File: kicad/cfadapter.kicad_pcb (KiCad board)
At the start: 2 copper layers, 66.9 x 60.4 mm, 5 parts, among them CON1 CF-CARD, J1 Extension port, U1 GAL16V8

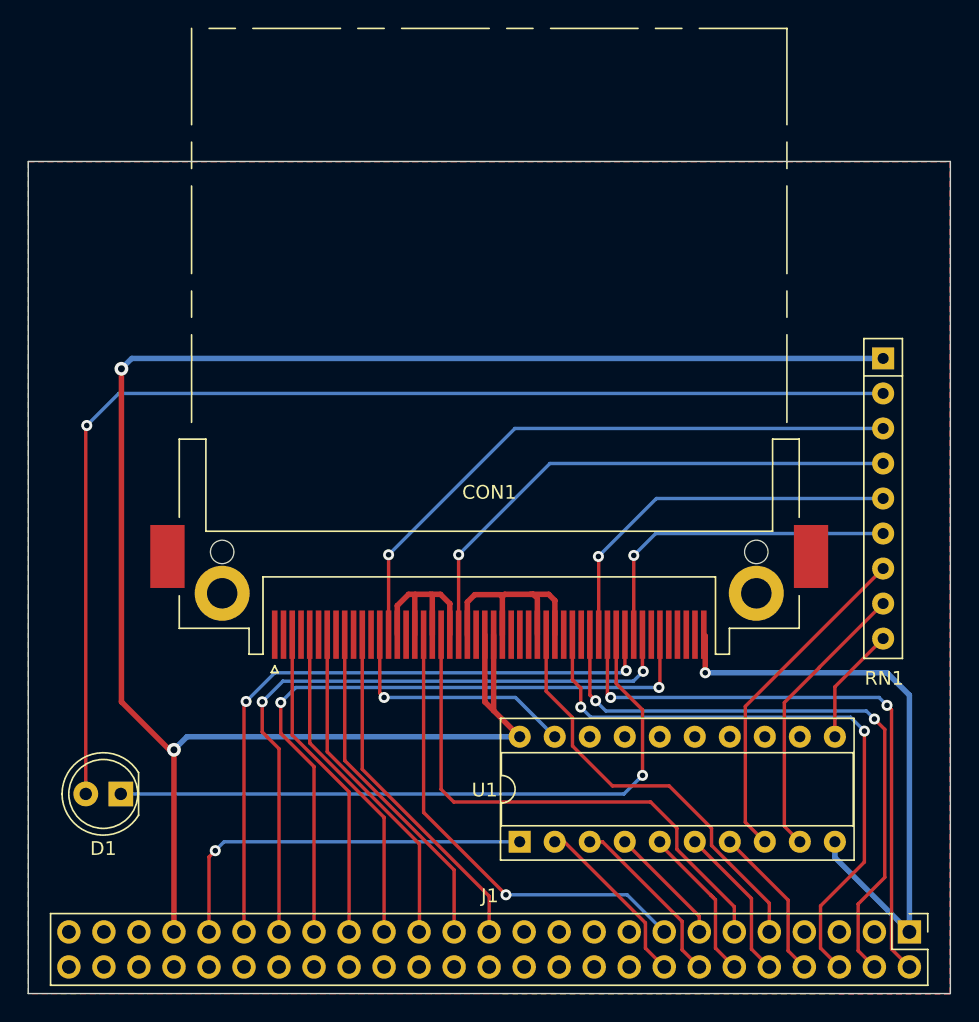
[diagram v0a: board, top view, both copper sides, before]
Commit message: kicad: Update the PCB to the manufactured v1.0.0
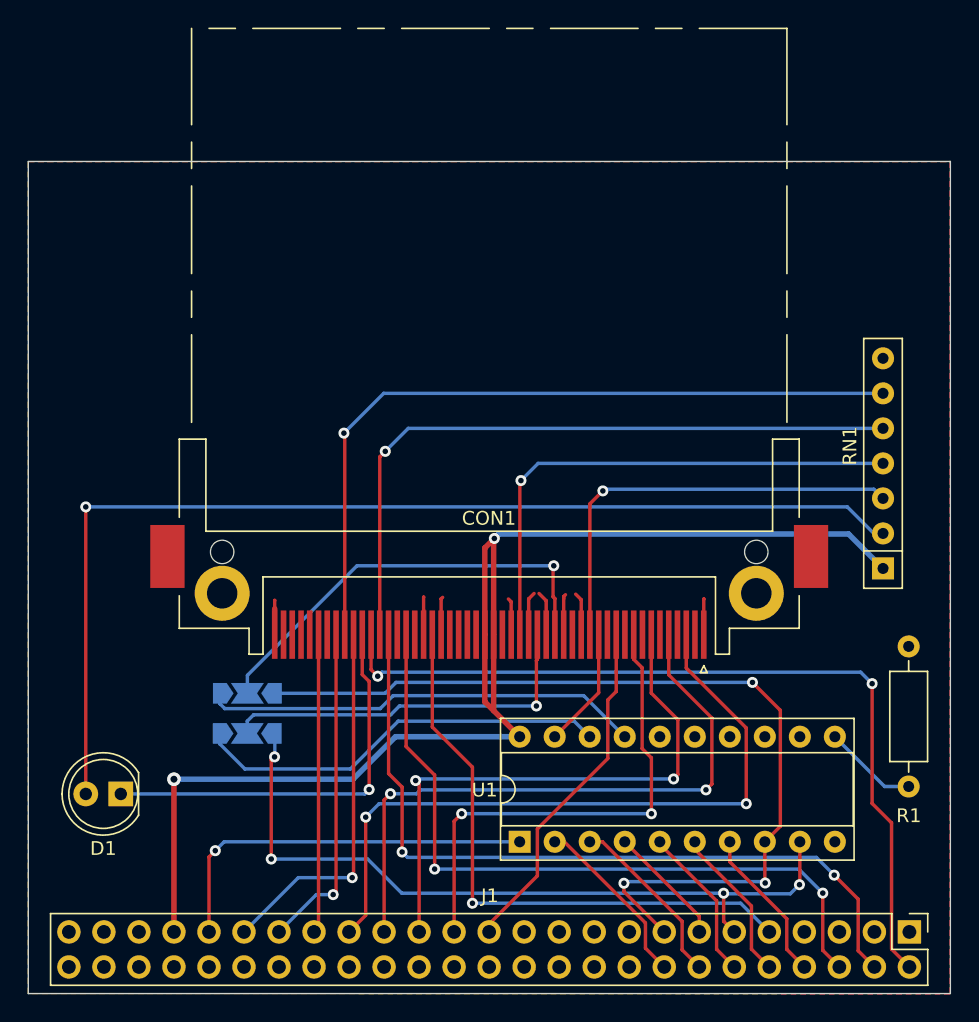
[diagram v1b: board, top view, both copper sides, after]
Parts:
- added JP1: RD_Choice, Jumper:SolderJumper-3_P2.0mm_Open_TrianglePad1.0x1.5mm_NumberLabels, B.Cu at (38.9, 74.2)
- added JP2: RD_Choice, Jumper:SolderJumper-3_P2.0mm_Open_TrianglePad1.0x1.5mm_NumberLabels, B.Cu at (38.9, 77.1)
- added R1: Pull-Down, Resistor_THT:R_Axial_DIN0207_L6.3mm_D2.5mm_P10.16mm_Horizontal, F.Cu at (86.8, 81.0)
- CON1: footprint Connector_Card:CF-Card_3M_N7E50-A516xx-30 -> Connector_Card:CF-Card_3M_N7E50-E516xx-30
- RN1: value R_Network08 -> Pull-Up Resistors; footprint Resistor_THT:R_Array_SIP9 -> Resistor_THT:R_Array_SIP7
- moved RN1 15.2 mm to (85.0, 65.2), turned to 90 degrees
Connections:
- CON1 pad 34: /~{RD} -> Net-(CON1A-/IORD)
- CON1 pad 35: /~{WR} -> Net-(CON1A-/IOWR)
- RN1 pad 7: /PULL_UP5 -> unconnected-(RN1-R6-Pad7)
- U1 pad 11: /PULL_UP7 -> Net-(U1-I10/~{OE})
- U1 pad 14: unconnected-(U1-Pad14) -> /~{CS_LATCH}
- U1 pad 15: unconnected-(U1-Pad15) -> /~{WR_LATCH}
- U1 pad 16: unconnected-(U1-Pad16) -> /~{RD_LATCH}
- U1 pad 17: unconnected-(U1-Pad17) -> /~{RD_DELAY}
- U1 pad 18: unconnected-(U1-Pad18) -> /~{WR_DELAY}
- U1 pad 8: /PULL_UP5 -> /~{RD}
- U1 pad 9: /PULL_UP6 -> /~{WR}
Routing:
- net GND: track 76.8 -> 27.5 mm, vias 1 -> 0
- net VCC: track 137.6 -> 95.0 mm
- net /~{RD}: track 33.9 -> 65.9 mm, vias 1 -> 3
- net /~{RD_DELAY}: track 0.00 -> 31.9 mm
- net Net-(CON1A-/IORD): track 0.00 -> 31.9 mm, vias 0 -> 1
- net /PULL_UP3: track 24.5 -> 54.9 mm
- net /~{WR_DELAY}: track 0.00 -> 30.2 mm
- net /DATA_2: track 49.4 -> 21.7 mm, vias 2 -> 0
- net /DATA_3: track 23.3 -> 50.9 mm, vias 0 -> 2
- net Net-(CON1A-/IOWR): track 0.00 -> 27.5 mm, vias 0 -> 1
- net /PULL_UP5: track 24.5 -> 0.00 mm
- net /DATA_1: track 48.4 -> 24.0 mm, vias 2 -> 1
- net /PULL_UP1: track 28.1 -> 50.3 mm
- net /DATA_4: track 23.8 -> 45.9 mm, vias 0 -> 2
- net /DATA_0: track 47.9 -> 27.1 mm, vias 2 -> 1
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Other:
- board text added: "JLCJLCJLCJLC"
- board text added: "v1.0.0"
